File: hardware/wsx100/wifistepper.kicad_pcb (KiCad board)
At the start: 2 copper layers, 77.6 x 57.3 mm, 63 parts, among them J1 Barrel_Jack_Switch, J2 Screw_Terminal, J3 Conn_01x06, J4 Conn_01x09, J5 Conn_01x02, SW1 SW_SPST, U1 ESP-WROOM-02, U2 powerSTEP01, U3 MAX15062A, U4 ATECC508A

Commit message: Updated hardware and webpage
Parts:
- removed R0: 00, Resistor_SMD:R_0805_2012Metric_Pad1.15x1.40mm_HandSolder
- removed R2: 1.8K, Resistor_SMD:R_0603_1608Metric
- added JP0: SolderJumper_2_Bridged, Jumper:SolderJumper-2_P1.3mm_Bridged_RoundedPad1.0x1.5mm, F.Cu at (83.1, 99.1)
- added JP3: SolderJumper_2_Bridged, Jumper:SolderJumper-2_P1.3mm_Bridged_RoundedPad1.0x1.5mm, F.Cu at (100.9, 93.0)
- added JP4: SolderJumper_3_Bridged12, Jumper:SolderJumper-3_P1.3mm_Bridged12_RoundedPad1.0x1.5mm, F.Cu at (52.0, 82.6)
- added R3: 47K, Resistor_SMD:R_0603_1608Metric, F.Cu at (50.3, 79.5)
- added R4: 1.8K, Resistor_SMD:R_0603_1608Metric, F.Cu at (48.6, 79.5)
- added R5: 2.2K, Resistor_SMD:R_0603_1608Metric, F.Cu at (104.9, 110.9)
- added R6: 1K, Resistor_SMD:R_0603_1608Metric, F.Cu at (105.0, 103.9)
- J4: value Conn_01x09 -> Conn_01x10; footprint Connector_PinHeader_2.54mm:PinHeader_1x09_P2.54mm_Vertical -> Connector_PinHeader_2.54mm:PinHeader_1x10_P2.54mm_Vertical
- R1: value 47K -> -; footprint Resistor_SMD:R_0603_1608Metric -> Resistor_SMD:R_0805_2012Metric_Pad1.15x1.40mm_HandSolder
- R14, R15: value 4.7K -> 2.2K
- RS1, RS2, RS3, RS4, RS5, RS6: value 0.06 -> 0.3
- moved R1 3.46 mm to (52.1, 79.2)
- moved C19 1.98 mm to (82.0, 107.8)
- moved R10 1.56 mm to (107.1, 95.4)
- moved RS1 1.52 mm to (59.3, 70.5)
- moved RS2 1.52 mm to (63.4, 70.5)
- moved RS3 1.52 mm to (67.4, 70.5)
- moved C8 1.46 mm to (55.8, 72.6)
- moved C18 1.02 mm to (78.3, 97.0)
- moved C5 0.70 mm to (48.6, 82.6), turned to 270 degrees
- moved U1 0.21 mm to (91.2, 80.7)
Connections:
- J4 pad 6: WIFI_ADC -> Net-(J4-Pad6)
- J4 pad 7: PROG_BOOT -> WIFI_GPIO
- J4 pad 8: PROG_RX -> PROG_BOOT
- J4 pad 9: PROG_TX -> PROG_RX
- R1 pad 2: SM_ADC -> Net-(JP4-Pad3)
- SW1 pad 2: AUTH_SDA -> AUTH_SCK
- U1 pad 17: WIFI_CONN -> WIFI_GPIO
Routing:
- net WIFI_GPIO: track 0.00 -> 38.8 mm, vias 0 -> 3
- net Net-(J4-Pad6): track 0.00 -> 17.1 mm
- net WIFI_ADC: track 38.3 -> 26.0 mm
- net AUTH_SCK: track 49.8 -> 57.8 mm, vias 2 -> 4
- net AUTH_SDA: track 70.4 -> 64.7 mm
- net SM_ADC: track 10.9 -> 16.0 mm
- net Net-(C19-Pad1): track 0.00 -> 3.16 mm
- net Net-(JP4-Pad3): track 0.00 -> 2.90 mm
- net PROG_BOOT: track 57.5 -> 54.8 mm
- net Net-(JP4-Pad1): track 0.00 -> 2.48 mm
- net Net-(JP0-Pad2): track 0.00 -> 2.13 mm
- net VIN: track 45.8 -> 47.9 mm, vias 66 -> 68
- net GND: track 22.8 -> 24.5 mm, vias 248 -> 218
- net WIFI_CONN: track 7.54 -> 6.24 mm
- net Net-(D4-Pad1): track 8.19 -> 6.93 mm
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- removed copper zone on F.Cu, net Net-(C19-Pad1)
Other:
- board text added: "3V3 GND SCK SDA RST ADC GPIO BOOT RX TX"
- board text added: "Good Robotics (2019)"
- board text added: "WSX100 RevC"
- board text removed: "3V3 GND SCK SDA RST ADC BOOT RX TX"
- board text removed: "Good Robotics (2018)"
- board text removed: "WSX100 RevB"

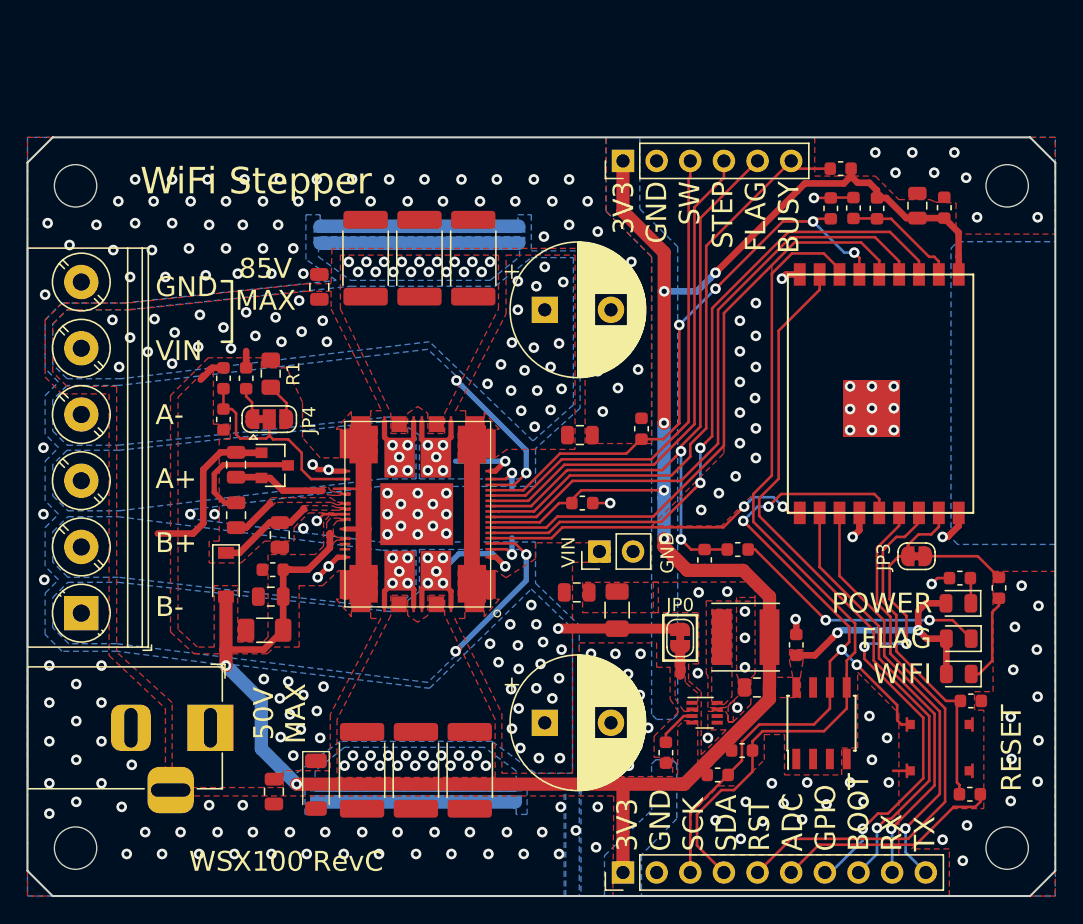
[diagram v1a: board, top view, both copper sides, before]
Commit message: Updated hardware to revD (still WIP)
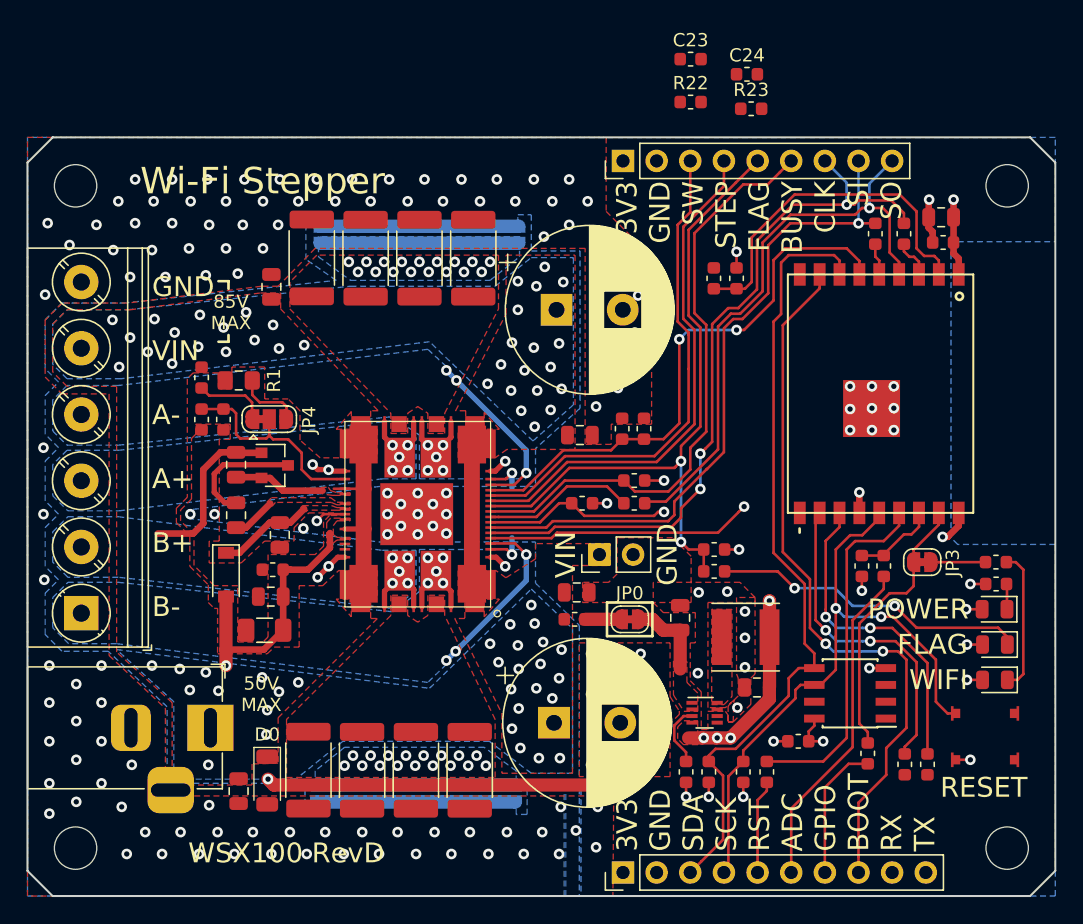
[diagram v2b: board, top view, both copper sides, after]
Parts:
- added C23: 1uF, Capacitor_SMD:C_0603_1608Metric, F.Cu at (83.8, 55.4)
- added C24: 0.1uF, Capacitor_SMD:C_0603_1608Metric, F.Cu at (88.1, 56.6)
- added FB1: Ferrite_Bead_Small, Inductor_SMD:L_0603_1608Metric, F.Cu at (75.1, 97.7)
- added R16: 22, Resistor_SMD:R_0603_1608Metric, F.Cu at (99.9, 68.6)
- added R17: 22, Resistor_SMD:R_0603_1608Metric, F.Cu at (97.8, 68.6)
- added R18: 22, Resistor_SMD:R_0603_1608Metric, F.Cu at (89.6, 109.2)
- added R19: 22, Resistor_SMD:R_0603_1608Metric, F.Cu at (97.2, 107.8)
- added R2: 22, Resistor_SMD:R_0603_1608Metric, F.Cu at (79.6, 89.0)
- added R20: 22, Resistor_SMD:R_0603_1608Metric, F.Cu at (100.0, 108.7)
- added R21: 22, Resistor_SMD:R_0603_1608Metric, F.Cu at (101.7, 108.7)
- added R22: 1K, Resistor_SMD:R_0603_1608Metric, F.Cu at (83.8, 58.7)
- added R23: 22, Resistor_SMD:R_0603_1608Metric, F.Cu at (88.4, 59.2)
- added RS7: 0.27, Resistor_SMD:R_2512_6332Metric, F.Cu at (55.2, 70.4)
- added RS8: 0.27, Resistor_SMD:R_2512_6332Metric, F.Cu at (55.0, 109.1)
- C10, C11: footprint Capacitor_THT:CP_Radial_D10.0mm_P5.00mm -> Capacitor_THT:CP_Radial_D12.5mm_P5.00mm
- C18: footprint Capacitor_SMD:C_1206_3216Metric -> Capacitor_SMD:C_0805_2012Metric
- J3: value Conn_01x06 -> Conn_01x09; footprint Connector_PinHeader_2.54mm:PinHeader_1x06_P2.54mm_Vertical -> Connector_PinHeader_2.54mm:PinHeader_1x09_P2.54mm_Vertical
- RS1, RS2, RS3, RS4, RS5, RS6: value 0.3 -> 0.27
- moved R7 28.2 mm to (79.6, 87.2)
- moved R12 21.8 mm to (80.3, 83.3)
- moved R5 18.4 mm to (98.4, 93.7), turned to 90 degrees
- moved R13 13.4 mm to (85.6, 72.0)
- moved R6 13.1 mm to (96.8, 93.7), turned to 270 degrees
- moved C17 10.3 mm to (87.3, 72.0)
- moved C21 7.28 mm to (92.0, 106.9), turned to 0 degrees
- moved C18 4.80 mm to (83.1, 97.6)
- moved JP0 4.05 mm to (79.3, 97.7), turned to 0 degrees
- moved D0 3.70 mm to (51.9, 109.9)
- moved C8 3.62 mm to (52.2, 72.6)
- moved SW1 3.52 mm to (106.1, 106.6)
- moved R4 3.52 mm to (46.9, 82.6), turned to 270 degrees
- moved R3 3.37 mm to (46.9, 79.5)
- moved U4 3.12 mm to (95.9, 103.3), turned to 180 degrees
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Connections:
- C18 pad 1: VIN -> Net-(C18-Pad1)
- J3 pad 3: SM_SW -> Net-(J3-Pad3)
- J3 pad 4: SM_STCLK -> Net-(J3-Pad4)
- J4 pad 10: PROG_TX -> Net-(J4-Pad10)
- J4 pad 3: AUTH_SCK -> AUTH_SDA
- J4 pad 4: AUTH_SDA -> AUTH_SCK
- J4 pad 5: WIFI_RST -> Net-(J4-Pad5)
- J4 pad 7: WIFI_GPIO -> Net-(J4-Pad7)
- J4 pad 9: PROG_RX -> Net-(J4-Pad9)
- JP0 pad 1: VIN -> Net-(FB1-Pad2)
- JP0 pad 2: Net-(JP0-Pad2) -> Net-(C18-Pad1)
- U1 pad 3: SM_CLK -> Net-(R16-Pad1)
- U1 pad 5: SM_SI -> Net-(R17-Pad1)
- U2 pad 14: SM_SO -> Net-(R2-Pad2)
- U3 pad 1: Net-(JP0-Pad2) -> Net-(C18-Pad1)
- U3 pad 2: Net-(JP0-Pad2) -> Net-(C18-Pad1)
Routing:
- net +3V3: track 190.7 -> 102.9 mm, vias 9 -> 16
- net WIFI_ADC: track 26.0 -> 6.31 mm
- net WIFI_GPIO: track 38.8 -> 20.9 mm, vias 3 -> 0
- net Net-(C17-Pad1): track 8.77 -> 26.7 mm
- net WIFI_RST: track 41.0 -> 26.7 mm
- net Net-(R2-Pad2): track 0.00 -> 11.5 mm
- net VIN: track 47.9 -> 37.4 mm, vias 68 -> 64
- net Net-(J4-Pad7): track 0.00 -> 10.1 mm
- net AUTH_SCK: track 57.8 -> 47.7 mm, vias 4 -> 2
- net Net-(J4-Pad6): track 17.1 -> 25.2 mm
- net PROG_TX: track 32.0 -> 24.3 mm, vias 1 -> 2
- net PROG_RX: track 32.1 -> 24.4 mm, vias 1 -> 2
- net Net-(J4-Pad5): track 0.00 -> 7.10 mm
- net Net-(C18-Pad1): track 0.00 -> 6.41 mm
- net SM_SI: track 45.7 -> 51.5 mm, vias 0 -> 1
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- added copper zone on In2.Cu, net +3V3
- added copper zone on In1.Cu, net GND
- added copper zone on In2.Cu, net GND
- added copper zone on F.Cu, net Net-(C18-Pad1)
- added copper zone on In1.Cu, net OUTA1
- added copper zone on In1.Cu, net OUTA2
- added copper zone on In1.Cu, net OUTB1
- added copper zone on In1.Cu, net OUTB2
- removed copper zone on F.Cu, net Net-(JP0-Pad2)
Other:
- copper layers 2 -> 4
- board text added: "3V3 GND SDA SCK RST ADC GPIO BOOT RX TX"
- board text added: "3V3 GND SW STEP FLAG BUSY CLK SI SO"
- board text added: "WSX100 RevD"
- board text added: "Wi-Fi Stepper"
- board text removed: "3V3 GND SCK SDA RST ADC GPIO BOOT RX TX"
- board text removed: "3V3 GND SW STEP FLAG BUSY"
- board text removed: "WSX100 RevC"
- board text removed: "WiFi Stepper"

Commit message: Updated Rev D
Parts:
- added D6: D_Zener, Diode_SMD:D_SOD-123, F.Cu at (87.0, 74.5)
- added REF**: OSHW-Logo2_7.3x6mm_SilkScreen, Symbol:OSHW-Logo2_7.3x6mm_SilkScreen, B.Cu at (46.6, 66.3)
- C10, C11: value 68uF 100V -> 100uF 100V (Low ESR)
- D0: value RPOL -> 80V (Back EMF Clamp); footprint Klofas-Passives:D_SOD80 -> Diode_SMD:D_SOD-123F
- moved R2 30.4 mm to (99.2, 65.8), turned to 0 degrees
- moved C23 16.2 mm to (85.3, 71.6), turned to 90 degrees
- moved C24 15.0 mm to (88.5, 71.6), turned to 90 degrees
- moved R13 13.9 mm to (99.2, 69.0), turned to 180 degrees
- moved R22 12.9 mm to (83.8, 71.6), turned to 270 degrees
- moved C17 12.8 mm to (99.2, 67.4), turned to 180 degrees
- moved R23 12.5 mm to (86.9, 71.6), turned to 270 degrees
- moved R16 6.23 mm to (94.0, 66.6), turned to 270 degrees
- moved R9 5.00 mm to (90.6, 93.8), turned to 90 degrees
- moved R5 3.88 mm to (95.9, 96.7)
- moved R6 3.88 mm to (94.3, 96.7)
- moved R8 3.61 mm to (89.0, 93.8), turned to 90 degrees
- moved R17 2.79 mm to (95.8, 66.6), turned to 270 degrees
- moved J5 1.78 mm to (78.7, 92.8)
- moved R19 1.37 mm to (98.3, 108.7)
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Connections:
- J3 pad 7: SM_CLK -> Net-(J3-Pad7)
- J3 pad 8: SM_SI -> Net-(J3-Pad8)
- J3 pad 9: SM_SO -> Net-(J3-Pad9)
- R16 pad 1: Net-(R16-Pad1) -> Net-(J3-Pad7)
- R17 pad 1: Net-(R17-Pad1) -> Net-(J3-Pad8)
- R2 pad 1: SM_SO -> Net-(J3-Pad9)
- R2 pad 2: Net-(R2-Pad2) -> SM_SO
- U1 pad 3: Net-(R16-Pad1) -> SM_CLK
- U1 pad 5: Net-(R17-Pad1) -> SM_SI
- U2 pad 14: Net-(R2-Pad2) -> SM_SO
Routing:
- net Net-(C17-Pad1): track 26.7 -> 6.14 mm
- net SM_CS: track 20.1 -> 34.4 mm, vias 1 -> 0
- net Net-(R2-Pad2): track 11.5 -> 0.00 mm
- net Net-(J3-Pad4): track 0.00 -> 7.92 mm
- net Net-(J4-Pad9): track 0.00 -> 7.77 mm
- net Net-(J3-Pad3): track 0.00 -> 7.71 mm
- net Net-(J4-Pad10): track 0.00 -> 7.43 mm
- net WIFI_GPIO: track 20.9 -> 28.0 mm
- net WIFI_ADC: track 6.31 -> 12.6 mm, vias 0 -> 2
- net SM_STCLK: track 39.3 -> 33.0 mm
- net GND: track 24.8 -> 30.8 mm, vias 166 -> 220
- net SM_SI: track 51.5 -> 46.1 mm, vias 1 -> 0
- net SM_FLAG: track 51.3 -> 56.6 mm
- net SM_SW: track 37.7 -> 32.8 mm
- net AUTH_SCK: track 47.7 -> 52.0 mm
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- added copper zone on In1.Cu, net VIN
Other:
- board text added: "+"
- board text added: "3V3 GND SW STEP FLAG BUSY"
- board text added: "3V3 GND SW STEP FLAG BUSY CLK MOSI MISO"
- board text added: "80V MAX"
- board text added: "GND A- A+ B+ B-"
- board text added: "WSX100 Rev D"
- board text removed: "3V3 GND SW STEP FLAG BUSY CLK SI SO"
- board text removed: "85V MAX"
- board text removed: "GND VIN A- A+ B+ B-"
- board text removed: "WSX100 RevD"

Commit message: final tweaks on Rev D
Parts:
- added R24: 22, Resistor_SMD:R_0603_1608Metric, F.Cu at (88.4, 72.2)
- added R25: 22, Resistor_SMD:R_0603_1608Metric, F.Cu at (88.4, 70.6)
- added R26: 22, Resistor_SMD:R_0603_1608Metric, F.Cu at (86.9, 109.2)
- added R27: 22, Resistor_SMD:R_0603_1608Metric, F.Cu at (88.6, 109.2)
- added R28: 22, Resistor_SMD:R_0603_1608Metric, F.Cu at (97.2, 99.4)
- C23: value 1uF -> 0.1uF
- D6: value D_Zener -> 3.9V
- R1: footprint Resistor_SMD:R_0805_2012Metric_Pad1.15x1.40mm_HandSolder -> Klofas-Passives:Resistor_NP_0805
- moved D0 38.1 mm to (52.0, 72.1), turned to 90 degrees
- moved D6 3.58 mm to (85.3, 77.7), turned to 180 degrees
- moved C23 3.41 mm to (83.7, 74.6)
- moved R22 3.35 mm to (85.3, 74.6)
- moved C24 2.98 mm to (88.5, 74.6), turned to 270 degrees
- moved R23 2.98 mm to (86.9, 74.6)
- moved R15 2.48 mm to (90.3, 109.2)
- moved R18 2.48 mm to (92.1, 109.2)
- moved C8 2.41 mm to (49.8, 72.6)
- moved C9 2.23 mm to (51.9, 110.6)
- moved R19 0.79 mm to (97.5, 108.5)
- moved R20 0.79 mm to (99.3, 108.5)
- moved R21 0.79 mm to (101.0, 108.5)
- moved D2 0.25 mm to (49.0, 94.4)
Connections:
- J3 pad 5: SM_FLAG -> Net-(J3-Pad5)
- J3 pad 6: SM_BUSY -> Net-(J3-Pad6)
- J4 pad 3: AUTH_SDA -> Net-(J4-Pad3)
- J4 pad 4: AUTH_SCK -> Net-(J4-Pad4)
- J4 pad 8: PROG_BOOT -> Net-(J4-Pad8)
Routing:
- net GND: track 30.8 -> 79.6 mm, vias 220 -> 216
- net PROG_BOOT: track 53.7 -> 33.0 mm
- net Net-(J4-Pad8): track 0.00 -> 17.8 mm
- net Net-(J3-Pad5): track 0.00 -> 10.3 mm
- net AUTH_SDA: track 59.2 -> 49.1 mm
- net SM_FLAG: track 56.6 -> 47.2 mm
- net Net-(J3-Pad6): track 0.00 -> 9.09 mm
- net Net-(J4-Pad3): track 0.00 -> 8.07 mm
- net AUTH_SCK: track 52.0 -> 43.9 mm
- net SM_BUSY: track 43.9 -> 35.9 mm
- net Net-(J4-Pad4): track 0.00 -> 7.75 mm
- net +3V3: track 106.0 -> 98.3 mm, vias 18 -> 16
- net Net-(J3-Pad3): track 7.71 -> 11.3 mm
- net Net-(J3-Pad4): track 7.92 -> 10.9 mm
- net WIFI_RST: track 28.9 -> 26.1 mm
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- added copper zone on In2.Cu, net OUTA1
- added copper zone on In2.Cu, net OUTA2
- added copper zone on In2.Cu, net OUTB1
- added copper zone on In2.Cu, net OUTB2
- added copper zone on In2.Cu, net VIN
- removed copper zone on In1.Cu, net OUTA1
- removed copper zone on In1.Cu, net OUTA2
- removed copper zone on In1.Cu, net OUTB1
- removed copper zone on In1.Cu, net OUTB2
- removed copper zone on In1.Cu, net VIN

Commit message: Nearing final Rev D
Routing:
- net GND: track 79.6 -> 75.6 mm, vias 216 -> 203

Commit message: Updated board layout
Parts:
- added D7: 50V Clamp, Klofas-Passives:D_SMF_DO-219AB, F.Cu at (83.4, 97.2)
- added R29: 22, Resistor_SMD:R_0603_1608Metric, F.Cu at (101.2, 65.9)
- D0: footprint Diode_SMD:D_SOD-123F -> Diode_SMD:D_SMB
- J3: value Conn_01x09 -> Conn_01x10; footprint Connector_PinHeader_2.54mm:PinHeader_1x09_P2.54mm_Vertical -> Connector_PinHeader_2.54mm:PinHeader_1x10_P2.54mm_Vertical
- moved C18 3.89 mm to (83.4, 101.5)
- moved C23 3.17 mm to (83.6, 71.4)
- moved C8 2.29 mm to (47.5, 72.5)
- moved D0 1.87 mm to (50.9, 70.6)
- moved C17 1.53 mm to (97.7, 67.5)
- moved R13 1.53 mm to (97.7, 69.1)
- moved R2 1.53 mm to (97.7, 65.9)
- moved R24 1.02 mm to (87.4, 72.2)
- moved R25 1.02 mm to (87.4, 70.6)
- moved R17 0.95 mm to (94.9, 66.6)
- moved R16 0.83 mm to (93.2, 66.6)
- moved C24 0.71 mm to (87.8, 74.7)
- moved R22 0.71 mm to (84.6, 74.7)
- moved R23 0.71 mm to (86.2, 74.7)
- moved C16 0.50 mm to (103.3, 69.6)
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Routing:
- net SM_CS: track 33.9 -> 60.3 mm, vias 0 -> 4
- net Net-(C18-Pad1): track 6.41 -> 1.79 mm
- net Net-(J3-Pad10): track 0.00 -> 2.95 mm
- net SM_SW: track 30.1 -> 32.3 mm
- net Net-(J3-Pad6): track 9.09 -> 10.5 mm
- net GND: track 75.6 -> 76.8 mm, vias 203 -> 192
- net Net-(C17-Pad1): track 6.14 -> 7.13 mm
- net Net-(J3-Pad4): track 10.9 -> 11.7 mm
- net Net-(J3-Pad9): track 2.93 -> 3.69 mm
- net SM_SI: track 45.7 -> 46.3 mm
- net Net-(J3-Pad5): track 10.3 -> 10.9 mm
- net AUTH_SDA: track 49.1 -> 49.6 mm
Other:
- net class +3V3 removed
- board text added: "3V3 GND SW STEP FLAG BUSY CLK MOSI MISO CS"
- board text added: "A- A+ B+ B-"
- board text removed: "3V3 GND SW STEP FLAG BUSY CLK MOSI MISO"
- board text removed: "GND A- A+ B+ B-"

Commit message: Updated hardware to rev d2
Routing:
- net GND: track 76.8 -> 38.4 mm, vias 192 -> 189
- net VIN: vias 44 -> 49
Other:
- board text added: "3V3 GND SDA SCL RST ADC GPIO BOOT RX TX"
- board text added: "WSX100 Rev D2"
- board text added: "wifistepper.com"
- board text removed: "3V3 GND SDA SCK RST ADC GPIO BOOT RX TX"
- board text removed: "WSX100 Rev D"
